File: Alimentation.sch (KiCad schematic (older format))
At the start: 37 parts, among them P1 Prise_Batterie, P2 Prise_Equilibrage, P3 Prise_Alimentation, P4 CONN_01X02, P5 CONN_01X02, P6 ConnecteurBippeur, P7 Serial Wire, U1 LD1084V, U2 STM32F303K8, U3 LD1117S50TR, U4 LD1117S33TR, U5 MCP2562-E/SN

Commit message: fin du schéma ?
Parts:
- removed C1, C3: 100n, symbol C
- removed C2, C4: 10µ, symbol C
- removed D1, D3, D5, D6: LED, symbol LED
- removed D4: DiodeProtection, symbol D_ALT
- removed F2: Fuse, symbol Fuse
- removed P3: Prise_Alimentation, symbol CONN_01X02
- removed P7: Serial Wire, symbol CONN_01X06
- removed R1, R2, R5, R6: R, symbol R
- removed R3: 744, symbol R
- removed U2: STM32F303K8, symbol STM32F303K8
- removed U3: LD1117S50TR, SOT-223, symbol LD1117S50TR
- removed U4: LD1117S33TR, SOT-223, symbol LD1117S33TR
- removed U5: MCP2562-E/SN, Housings_SOIC:SOIC-8_3.9x4.9mm_Pitch1.27mm, symbol MCP2562-E/SN
- added C?: 10µ, symbol C
- added P2: Prise_Batterie, symbol CONN_01X02
- added P5: CONN_01X04, symbol CONN_01X04
- added P6: CONN_01X02, symbol CONN_01X02
- added RV?: POT, symbol POT
- D3: renamed from D7; symbol LED -> LED-RESCUE-Alimentation
- D4: renamed from D8; symbol LED -> LED-RESCUE-Alimentation
- renumbered C6 to C1, C7 to C2, C5 to C3, P2 to P1, P1 to P3, P6 to P4, P4 to P7, P5 to P8, R4 to R3, R7 to R4, R8 to R5
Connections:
- net LedStatus is gone; now on net Non_régulé: R5.1
- net VCC is gone; now on net +9V: C1.1 (VCC), C2.1 (VCC), P8.1 (P1), R3.1, U1.2 (VO)
- net GND: now also C?.2, P2.1 (P1), P5.3 (P3), RV?.2, RV?.3; no longer P1.1 (P1), P4.5 (P5)
- net at D2.2 (A): now also C3.1, U1.3 (VI), P6.1 (P1)
- net at R3.2, U1.1 (ADJ): now also RV?.1
- net Non_régulé: now reaches P7.1 (P1)
- net Non_régulé: now also P6.2 (P2)
- net CAN_L: now reaches C1.3 (CAN_L), C2.3 (CAN_L)
- net CAN_H: now reaches C1.2 (CAN_H), C2.2 (CAN_H)
- net +3V3 renamed +9V
- net +9V: now also C?.1
- net +BATT: no longer names the net of P3.2 (P2)
- net +BATT: now also P5.2 (P2); no longer F1.2
- net ADC1_IN1: no longer names the net of P1.5 (P5), P4.1 (P1)
- net ADC1_IN2: no longer names the net of P1.4 (P4), P4.2 (P2)
- net ADC1_IN3: no longer names the net of P1.3 (P3), P4.3 (P3)
- net ADC1_IN4: no longer names the net of P1.2 (P2), P4.4 (P4)
- new net: P1.1 (P1), P4.5 (P5)
- new net: F1.2, P5.4 (P4)
- new net: P2.2 (P2), P5.1 (P1)
- no-connect marks 18 -> 0
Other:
- note added: "Alimentation stabilisée"
- note added: "Batterie"
- note added: "Puissance (non régulé)"
- note added: "Électronique (9V régulé)"
- note removed: "Alimentation"
- note removed: "Alimentation 5V + 3V3"
- note removed: "Batterie 4S"
- note removed: "Connexion au bus CAN + Alimentation"
- note removed: "Puissance (Batterie directe)"
- note removed: "Électronique (±9V)"
- moved on the sheet: C1, C2, C3, D2, D3, D4, F1, P1, P3, P4, P7, P8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

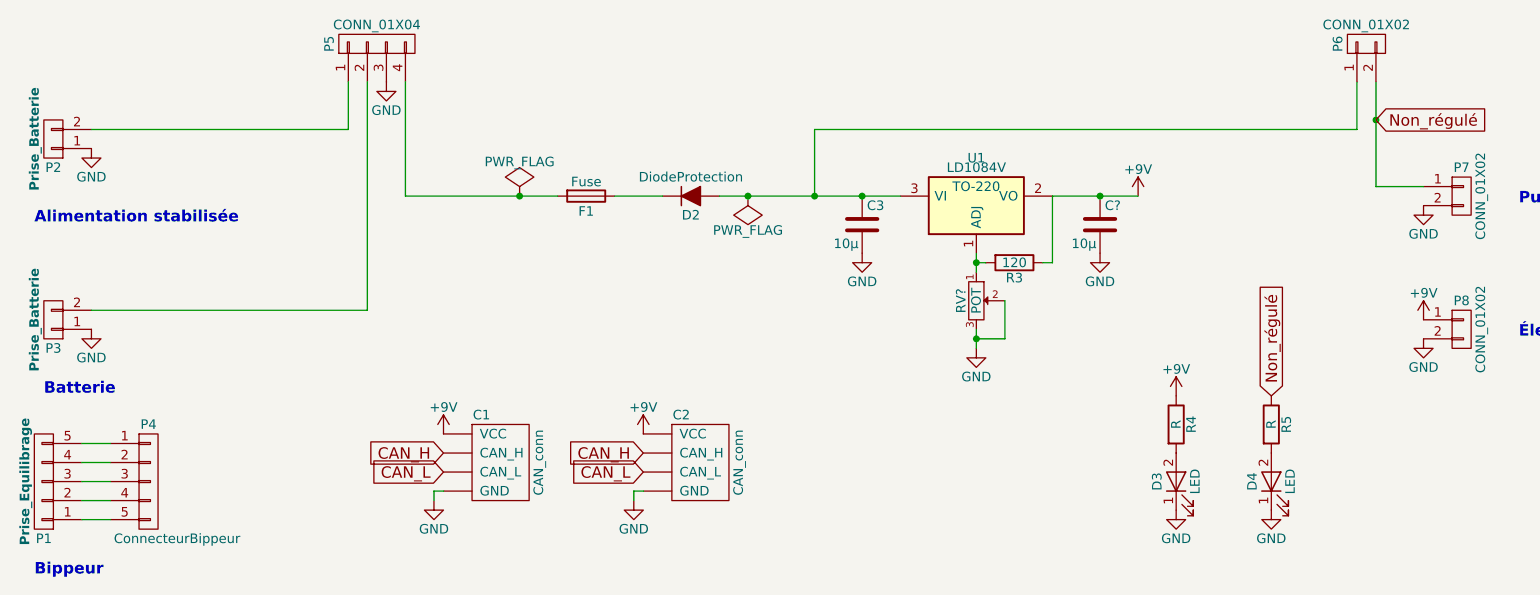
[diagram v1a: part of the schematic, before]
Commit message: association footprint + placement
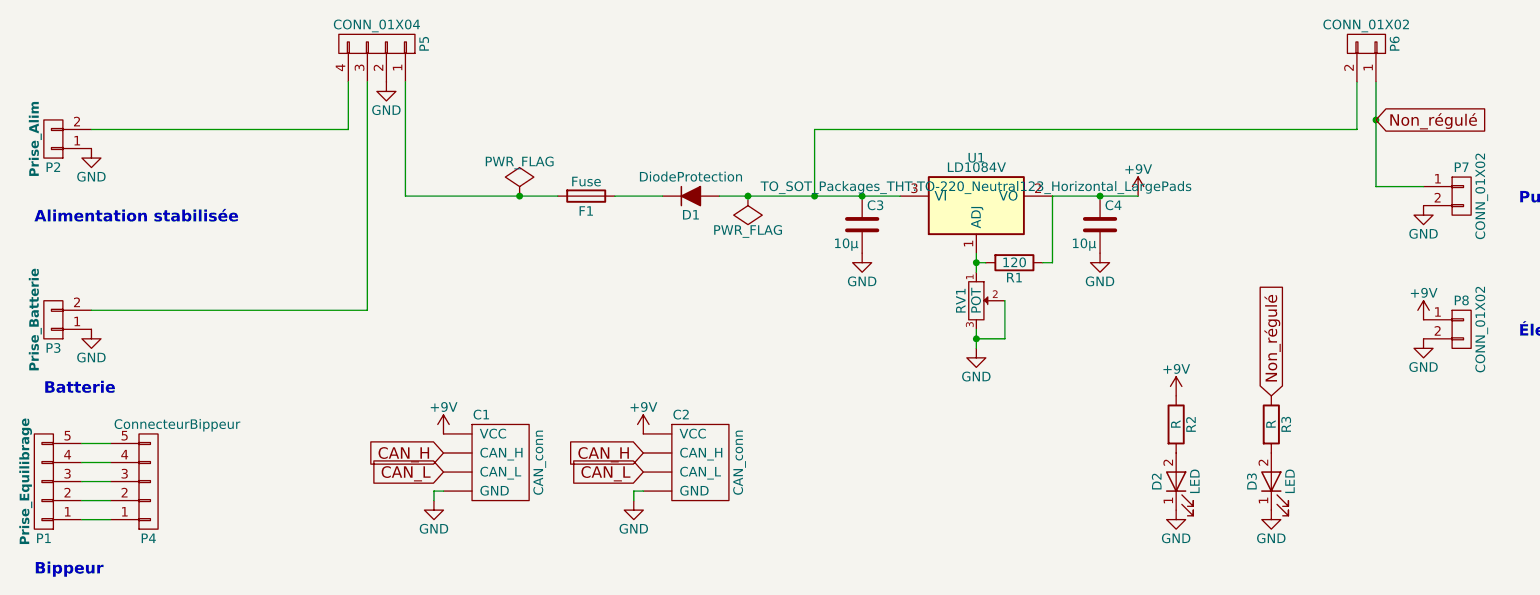
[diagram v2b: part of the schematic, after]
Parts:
- C1, C2: footprint (none) -> Connectors_JST:JST_XH_B04B-XH-A_04x2.50mm_Straight
- C3: footprint (none) -> Capacitors_SMD:C_0805_HandSoldering
- C4: renamed from C?; footprint (none) -> Capacitors_SMD:C_0805_HandSoldering
- D1: renamed from D2; footprint (none) -> Diodes_ThroughHole:Diode_DO-41_SOD81_Horizontal_RM10
- D2: renamed from D3; footprint (none) -> LEDs:LED_0805
- D3: renamed from D4; footprint (none) -> LEDs:LED_0805
- F1: footprint (none) -> Fuse_Holders_and_Fuses:Fuseholder5x20_horiz_open_Schurter_0031_8201
- P1: footprint (none) -> Connectors_JST:JST_XH_B05B-XH-A_05x2.50mm_Straight
- P2: value Prise_Batterie -> Prise_Alim; footprint (none) -> Connectors_Phoenix:PhoenixContact_MSTBVA-G_02x5.00mm_Vertical
- P3, P7, P8: footprint (none) -> Connectors_Phoenix:PhoenixContact_MSTBVA-G_02x5.00mm_Vertical
- P4: footprint (none) -> Pin_Headers:Pin_Header_Straight_1x05
- P5: footprint (none) -> Terminal_Blocks:TerminalBlock_Pheonix_MPT-2.54mm_4pol
- P6: footprint (none) -> Terminal_Blocks:TerminalBlock_Pheonix_MPT-2.54mm_2pol
- R1: renamed from R3; footprint (none) -> Resistors_SMD:R_0805_HandSoldering
- R2: renamed from R4; footprint (none) -> Resistors_SMD:R_0805_HandSoldering
- R3: renamed from R5; footprint (none) -> Resistors_SMD:R_0805_HandSoldering
- RV1: renamed from RV?; footprint (none) -> Potentiometers:Potentiometer_Bourns_3296W_3-8Zoll_Inline_ScrewUp
- U1: footprint TO-220 -> TO_SOT_Packages_THT:TO-220_Neutral123_Horizontal_LargePads
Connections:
- net GND: now also P5.2 (P2); no longer P5.3 (P3)
- net Non_régulé: now also P6.1 (P1); no longer P6.2 (P2)
- net at P1.1 (P1): now also P4.1 (P1); no longer P4.5 (P5)
- net at P1.2 (P2): now also P4.2 (P2); no longer P4.4 (P4)
- net at P1.4 (P4): now also P4.4 (P4); no longer P4.2 (P2)
- net at P1.5 (P5): now also P4.5 (P5); no longer P4.1 (P1)
- net at P3.2 (P2): now also P5.3 (P3); no longer P5.2 (P2)
- net at F1.2: now also P5.1 (P1); no longer P5.4 (P4)
- net at C3.1, D1.2 (A), U1.3 (VI): now also P6.2 (P2); no longer P6.1 (P1)
- net at P2.2 (P2): now also P5.4 (P4); no longer P5.1 (P1)

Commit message: prise en compte des changements dans la lib perso
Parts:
- removed C1, C2: CAN_conn, Connectors_JST:JST_XH_B04B-XH-A_04x2.50mm_Straight, symbol CAN_conn
- added P6, P7: CAN_conn, Connectors_JST:JST_XH_B04B-XH-A_04x2.50mm_Straight, symbol CAN_conn
- renumbered C3 to C1, C4 to C2, P8 to P10, P6 to P8, P7 to P9
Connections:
- net +9V: now also P6.1 (VCC), P7.1 (VCC)
- net CAN_H: now also P6.2 (CAN_H), P7.2 (CAN_H)
- net CAN_L: now also P6.3 (CAN_L), P7.3 (CAN_L)
- net GND: now also P6.4 (GND), P7.4 (GND)
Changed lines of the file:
@@
 Bippeur
 $Comp
-L CONN_01X02 P7
+L CONN_01X02 P9
 U 1 1 58851833
 P 9100 3100
-F 0 "P7" H 9100 3250 50  0000 C CNN
+F 0 "P9" H 9100 3250 50  0000 C CNN
 F 1 "CONN_01X02" V 9200 3100 50  0000 C CNN
 F 2 "Connectors_Phoenix:PhoenixContact_MSTBVA-G_02x5.00mm_Vertical" H 9100 3100 50  0001 C CNN
@@
 $EndComp
 $Comp
-L CONN_01X02 P8
+L CONN_01X02 P10
 U 1 1 58851912
 P 9100 3800
-F 0 "P8" H 9100 3950 50  0000 C CNN
+F 0 "P10" H 9100 3950 50  0000 C CNN
 F 1 "CONN_01X02" V 9200 3800 50  0000 C CNN
 F 2 "Connectors_Phoenix:PhoenixContact_MSTBVA-G_02x5.00mm_Vertical" H 9100 3800 50  0001 C CNN
@@
 $EndComp
 $Comp
-L C C3
+L C C1
 U 1 1 588536AF
 P 5950 3250
-F 0 "C3" H 5975 3350 50  0000 L CNN
+F 0 "C1" H 5975 3350 50  0000 L CNN
 F 1 "10µ" H 5800 3150 50  0000 L CNN
 F 2 "Capacitors_SMD:C_0805_HandSoldering" H 5988 3100 50  0001 C CNN
@@
 $EndComp
 $Comp
-L CAN_conn C1
-U 1 1 58854006
-P 3950 4500
-F 0 "C1" H 3950 4750 50  0000 C CNN
-F 1 "CAN_conn" V 4250 4500 50  0000 C CNN
-F 2 "Connectors_JST:JST_XH_B04B-XH-A_04x2.50mm_Straight" H 3950 4500 50  0001 C CNN
-F 3 "" H 3950 4500 50  0000 C CNN
-	1    3950 4500
-	1    0    0    -1
-$EndComp
-$Comp
 L GND #PWR05
 U 1 1 58854155
@@
 F 3 "" H 4750 4700 50  0000 C CNN
 	1    4750 4700
-	1    0    0    -1
-$EndComp
-$Comp
-L CAN_conn C2
-U 1 1 588543B3
-P 5000 4500
-F 0 "C2" H 5000 4750 50  0000 C CNN
-F 1 "CAN_conn" V 5300 4500 50  0000 C CNN
-F 2 "Connectors_JST:JST_XH_B04B-XH-A_04x2.50mm_Straight" H 5000 4500 50  0001 C CNN
-F 3 "" H 5000 4500 50  0000 C CNN
-	1    5000 4500
 	1    0    0    -1
 $EndComp
@@
 Connection ~ 5350 3100
 $Comp
-L CONN_01X02 P6
+L CONN_01X02 P8
 U 1 1 5892A99F
 P 8600 2300
-F 0 "P6" H 8600 2450 50  0000 C CNN
+F 0 "P8" H 8600 2450 50  0000 C CNN
 F 1 "CONN_01X02" V 8700 2300 50  0000 C CNN
 F 2 "Terminal_Blocks:TerminalBlock_Pheonix_MPT-2.54mm_2pol" H 8600 2300 50  0001 C CNN
@@
 $EndComp
 $Comp
-L C C4
+L C C2
 U 1 1 5892C9AC
 P 7200 3250
-F 0 "C4" H 7225 3350 50  0000 L CNN
+F 0 "C2" H 7225 3350 50  0000 L CNN
 F 1 "10µ" H 7050 3150 50  0000 L CNN
 F 2 "Capacitors_SMD:C_0805_HandSoldering" H 7238 3100 50  0001 C CNN
@@
 Connection ~ 6550 3850
 Connection ~ 5950 3100
+$Comp
+L CAN_conn P7
+U 1 1 5893CEA2
+P 5000 4500
+F 0 "P7" H 5000 4750 50  0000 C CNN
+F 1 "CAN_conn" V 5300 4500 50  0000 C CNN
+F 2 "Connectors_JST:JST_XH_B04B-XH-A_04x2.50mm_Straight" H 5000 4500 50  0001 C CNN
+F 3 "" H 5000 4500 50  0000 C CNN
+	1    5000 4500
+	1    0    0    -1
+$EndComp
+$Comp
+L CAN_conn P6
+U 1 1 5893CFB7
+P 3950 4500
+F 0 "P6" H 3950 4750 50  0000 C CNN
+F 1 "CAN_conn" V 4250 4500 50  0000 C CNN
+F 2 "Connectors_JST:JST_XH_B04B-XH-A_04x2.50mm_Straight" H 3950 4500 50  0001 C CNN
+F 3 "" H 3950 4500 50  0000 C CNN
+	1    3950 4500
+	1    0    0    -1
+$EndComp
 $EndSCHEMATC
